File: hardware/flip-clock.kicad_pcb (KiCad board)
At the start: 2 copper layers, 82.5 x 47.8 mm, 19 parts, among them J1 Screw_Terminal_01x02, J2 Conn_01x04, Q1 TCRT5000, U1 WeMos_D1_mini

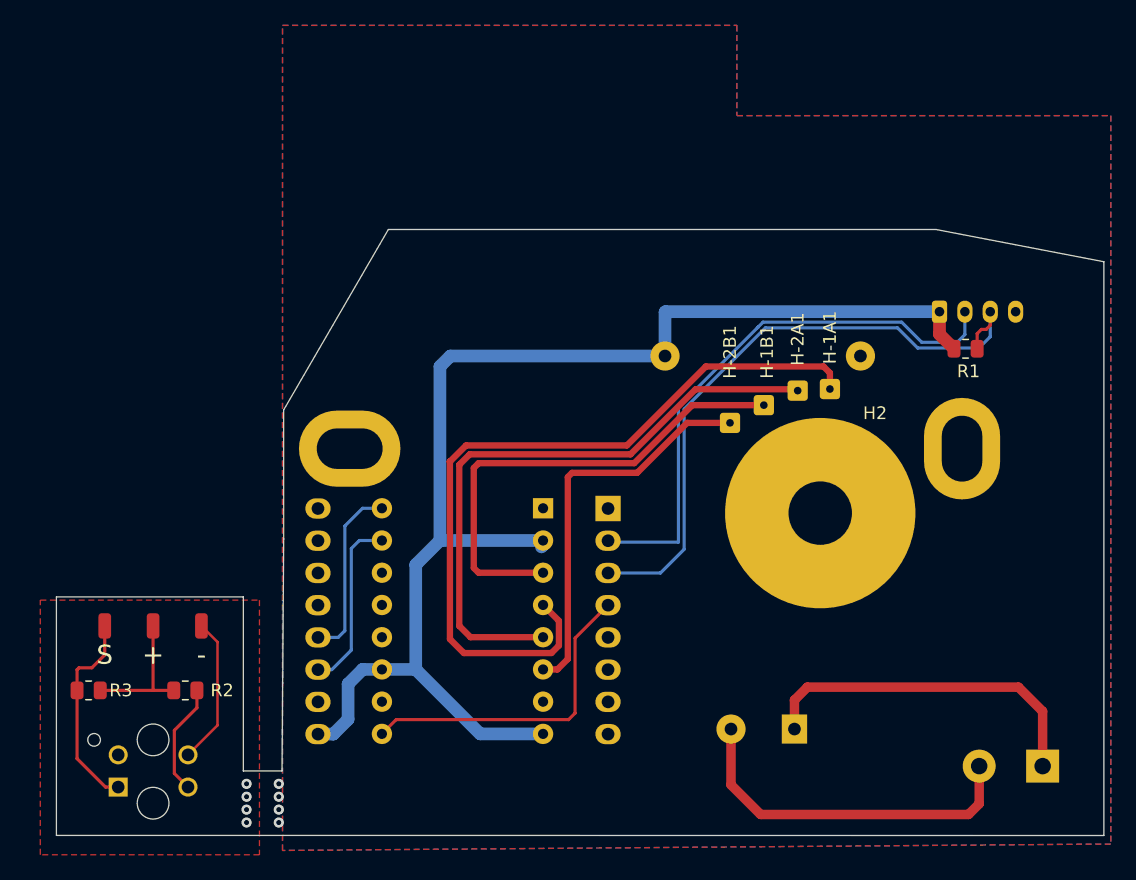
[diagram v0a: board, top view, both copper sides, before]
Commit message: Use 3v3 as stable power supply for IR-Sensor
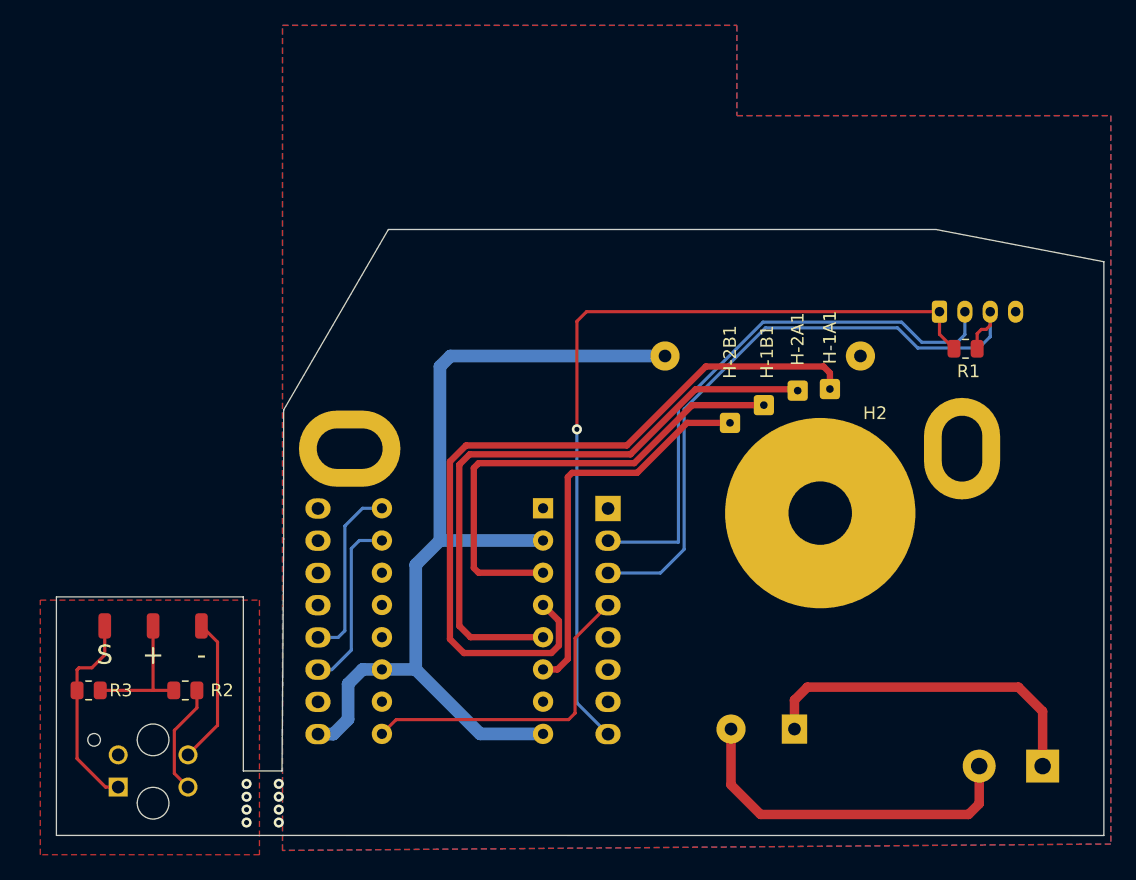
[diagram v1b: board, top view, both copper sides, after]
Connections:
- J2 pad 1: VCC -> +3V3
- R1 pad 1: VCC -> +3V3
- U1 pad 8: unconnected-(U1-Pad8) -> +3V3
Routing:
- net +3V3: track 0.00 -> 65.8 mm, vias 0 -> 1
- net VCC: track 103.5 -> 74.5 mm
- net /PD_IN: track 44.4 -> 43.5 mm

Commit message: Adds detection of rising and falling edge
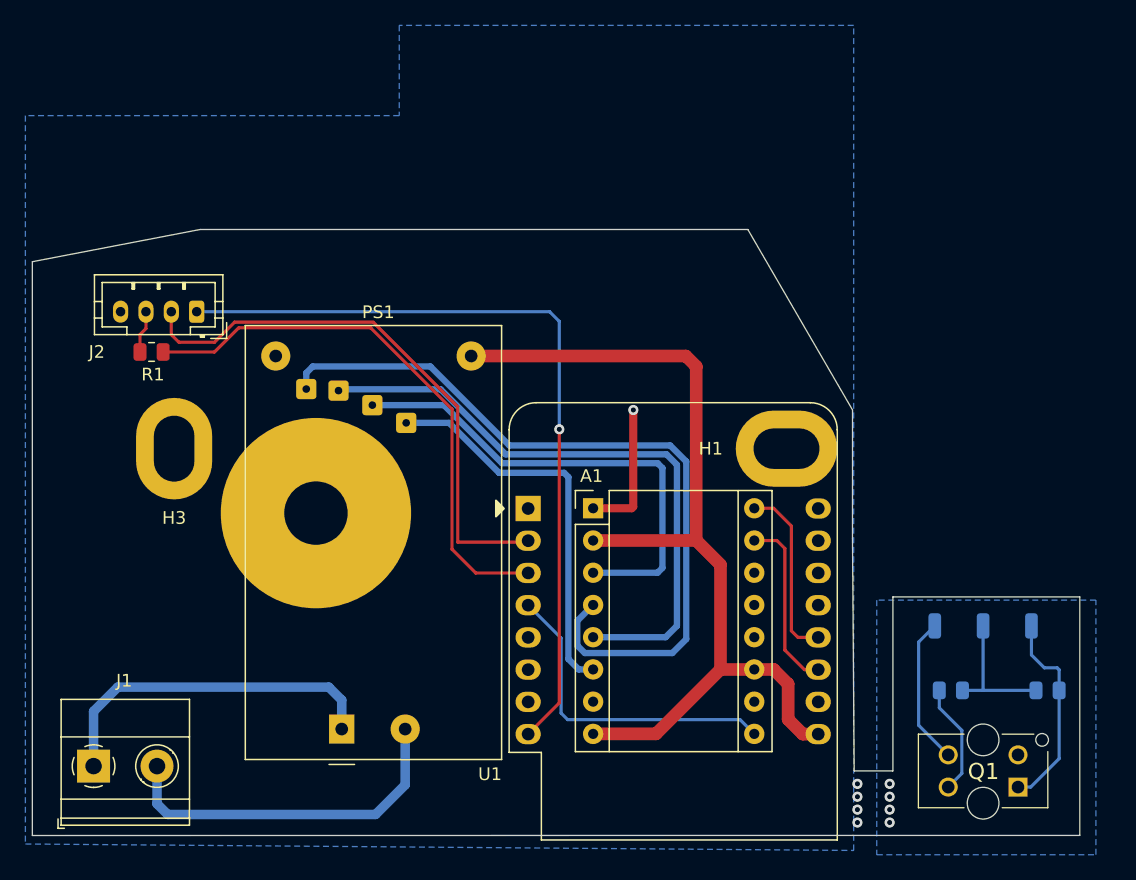
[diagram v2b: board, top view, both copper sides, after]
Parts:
- A1, H-1A1, H-1B1, H-2A1, H-2B1, H1, H3, J1, J2, PS1, Q1, U1: moved to F.Cu
- H2, H4, H5, H6, R3: moved to B.Cu
- R2: value 330 -> 56; moved to B.Cu
- moved R3 75.6 mm to (175.9, 74.9), turned to 180 degrees
- moved J1 74.8 mm to (100.7, 80.9), turned to 0 degrees
- moved H5 73.0 mm to (174.6, 69.8), turned to 0 degrees
- moved H4 65.4 mm to (170.8, 69.8), turned to 0 degrees
- moved Q1 65.4 mm to (170.8, 81.3), turned to 180 degrees
- moved R1 64.2 mm to (105.3, 48.3)
- moved H3 62.1 mm to (107.1, 55.9), turned to 0 degrees
- moved R2 60.3 mm to (168.3, 74.9), turned to 180 degrees
- moved J2 58.5 mm to (108.8, 45.1), turned to 180 degrees
- moved H6 57.8 mm to (167.0, 69.8), turned to 0 degrees
- moved H-1A1 41.5 mm to (117.4, 51.3), turned to 180 degrees
- moved H2 39.7 mm to (118.2, 61.0), turned to 180 degrees
- moved H-2A1 36.2 mm to (120.0, 51.3), turned to 180 degrees
- moved PS1 35.7 mm to (120.3, 78.0)
- moved H1 34.4 mm to (155.3, 55.9), turned to 0 degrees
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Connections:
- J2 pad 3: /HOUR -> Net-(J2-Pad3)
- R1 pad 1: +3V3 -> Net-(J2-Pad3)
- R1 pad 2: /HOUR -> Net-(R1-Pad2)
- U1 pad 3: /HOUR -> Net-(R1-Pad2)
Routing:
- net /HOUR: track 51.2 -> 0.00 mm
- net Net-(R1-Pad2): track 0.00 -> 44.0 mm
- net GND: track 0.00 -> 10.8 mm, vias 0 -> 1
- net +3V3: track 65.8 -> 62.4 mm
- net Net-(J2-Pad3): track 0.00 -> 3.37 mm
- added copper zone on B.Cu, net /-
- removed copper zone on F.Cu, net /-
- removed copper zone on F.Cu, net GND
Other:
- board size 82.5 x 47.8 mm -> 82.6 x 47.8 mm
